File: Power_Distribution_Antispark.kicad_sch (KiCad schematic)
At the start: 87 parts, among them J1 STM Signal Conn, J2 +48V Battery Conn, J3 Motor Conn, Q1 BUK9M42-60EX, Q2 G20P06K, Q3 BUK9M42-60EX, Q4 G20P06K, U1 TLV74033PDBVR, U2 74LVC1G14GW_125, U3 TPP60308-ES1R-S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

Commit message: component layout
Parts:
- added TP1, TP10, TP11, TP12, TP2, TP3, TP4, TP5, TP6, TP7, TP8, TP9: TestPoint, TestPoint:TestPoint_Pad_D1.0mm, symbol Connector:TestPoint
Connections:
- net +3V3: now also TP12.1
- net C_Sense_12V_1: now also TP8.1
- net C_Sense_12V_2: now also TP9.1
- net C_Sense_12V_3: now also TP10.1
- net C_Sense_3V3: now also TP4.1
- net C_Sense_3V3_STM: now also TP3.1
- net C_Sense_5V_1: now also TP5.1
- net C_Sense_5V_2: now also TP6.1
- net C_Sense_5V_3: now also TP7.1
- net PreCharge_Sense: now also TP11.1
- net V_S_12V_Output: now also TP1.1
- net V_S_5V_Output: now also TP2.1

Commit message: all traces
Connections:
- net C_Sense_12V_1: now also J1.6 (Pin_6); no longer J1.4 (Pin_4)
- net GND: now also J1.5 (Pin_5); no longer J1.6 (Pin_6)
- net V_S_12V_Output: now also J1.4 (Pin_4); no longer J1.5 (Pin_5)
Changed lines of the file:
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@@
 	)
 	(junction
-		(at 85.09 356.87)
-		(diameter 0)
-		(color 0 0 0 0)
-	)
-	(junction
 		(at 60.96 369.57)
 		(diameter 0)
@@
 	)
 	(junction
+		(at 35.56 349.25)
+		(diameter 0)
+		(color 0 0 0 0)
+	)
+	(junction
 		(at 231.14 137.16)
 		(diameter 0)
@@
 	(wire
 		(pts
-			(xy 35.56 346.71) (xy 35.56 354.33)
+			(xy 35.56 346.71) (xy 35.56 349.25)
 		)
 		(stroke
@@
 		)
 	)
-	(wire
-		(pts
-			(xy 85.09 349.25) (xy 67.31 349.25)
-		)
-		(stroke
-			(width 0)
-			(type default)
-		)
-	)
 	(polyline
 		(pts
@@
 	(wire
 		(pts
+			(xy 35.56 349.25) (xy 35.56 354.33)
+		)
+		(stroke
+			(width 0)
+			(type default)
+		)
+	)
+	(wire
+		(pts
 			(xy 66.04 142.24) (xy 68.58 142.24)
 		)
@@
 	(wire
 		(pts
-			(xy 85.09 356.87) (xy 85.09 349.25)
-		)
-		(stroke
-			(width 0)
-			(type default)
-		)
-	)
-	(wire
-		(pts
 			(xy 119.38 168.91) (xy 119.38 171.45)
 		)
@@
 	(wire
 		(pts
+			(xy 35.56 349.25) (xy 54.61 349.25)
+		)
+		(stroke
+			(width 0)
+			(type default)
+		)
+	)
+	(wire
+		(pts
 			(xy 369.57 356.87) (xy 369.57 363.22)
 		)
@@
 	)
 	(label "V_S_12V_Output"
-		(at 54.61 349.25 180)
+		(at 67.31 346.71 0)
 		(effects
 			(font
 				(size 1.27 1.27)
 			)
-			(justify right bottom)
+			(justify left bottom)
 		)
 	)
@@
 		)
 	)
-	(label "C_Sense_12V_1"
-		(at 67.31 346.71 0)
-		(effects
-			(font
-				(size 1.27 1.27)
-			)
-			(justify left bottom)
-		)
-	)
 	(label "C_Sense_12V_2"
 		(at 67.31 359.41 0)
@@
 		(effects
 			(font
+				(size 1.27 1.27)
+			)
+			(justify left bottom)
+		)
+	)
+	(label "C_Sense_12V_1"
+		(at 67.31 349.25 0)
+		(effects
+			(font

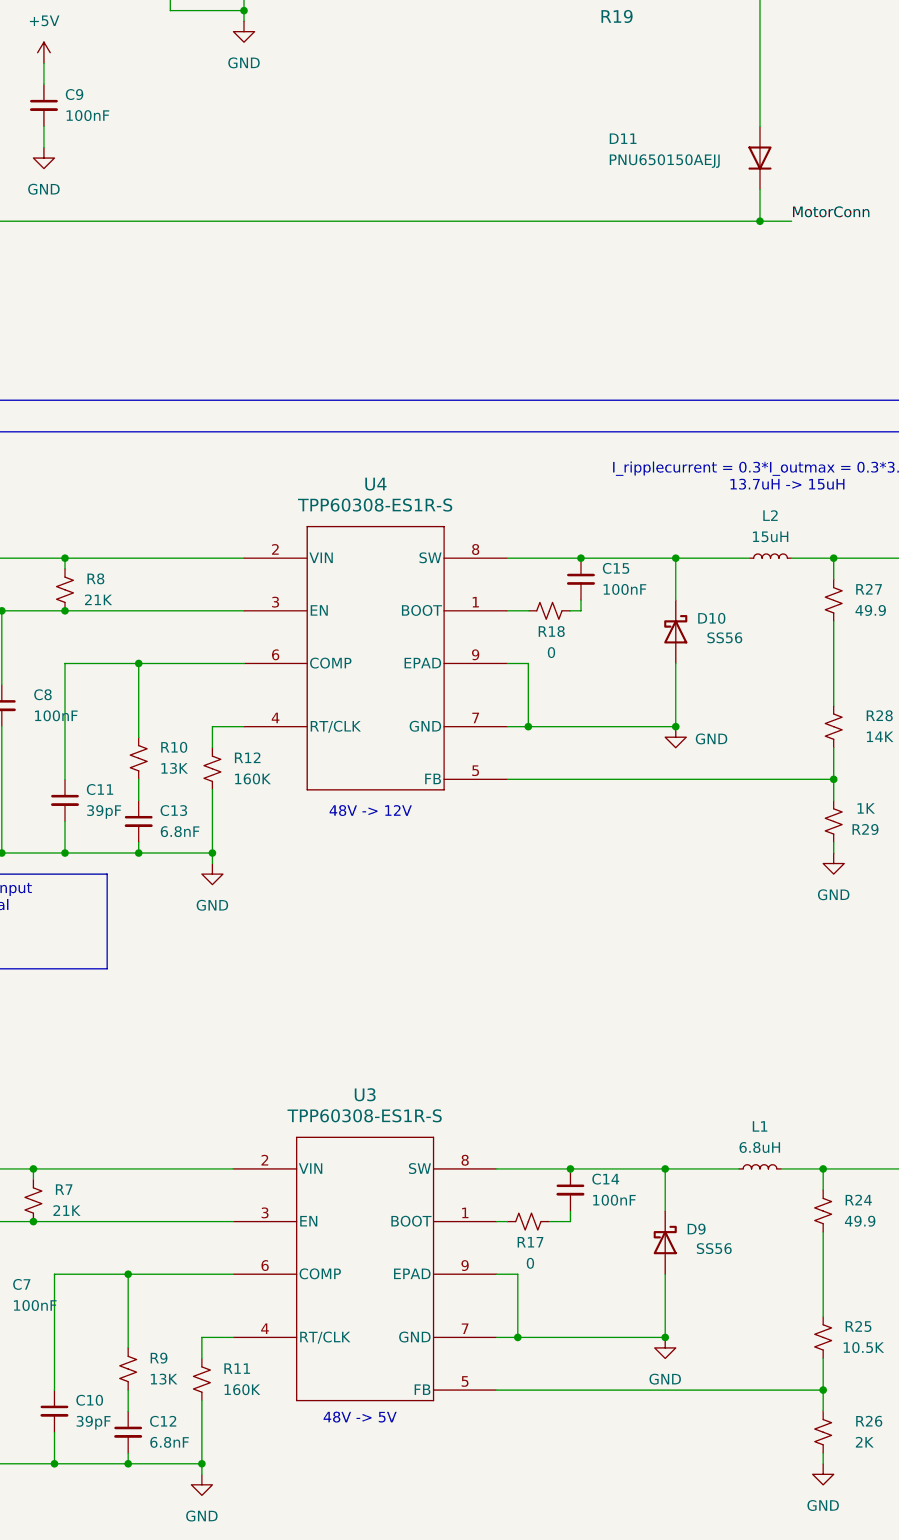
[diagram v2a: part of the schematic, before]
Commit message: fixed silkscreens
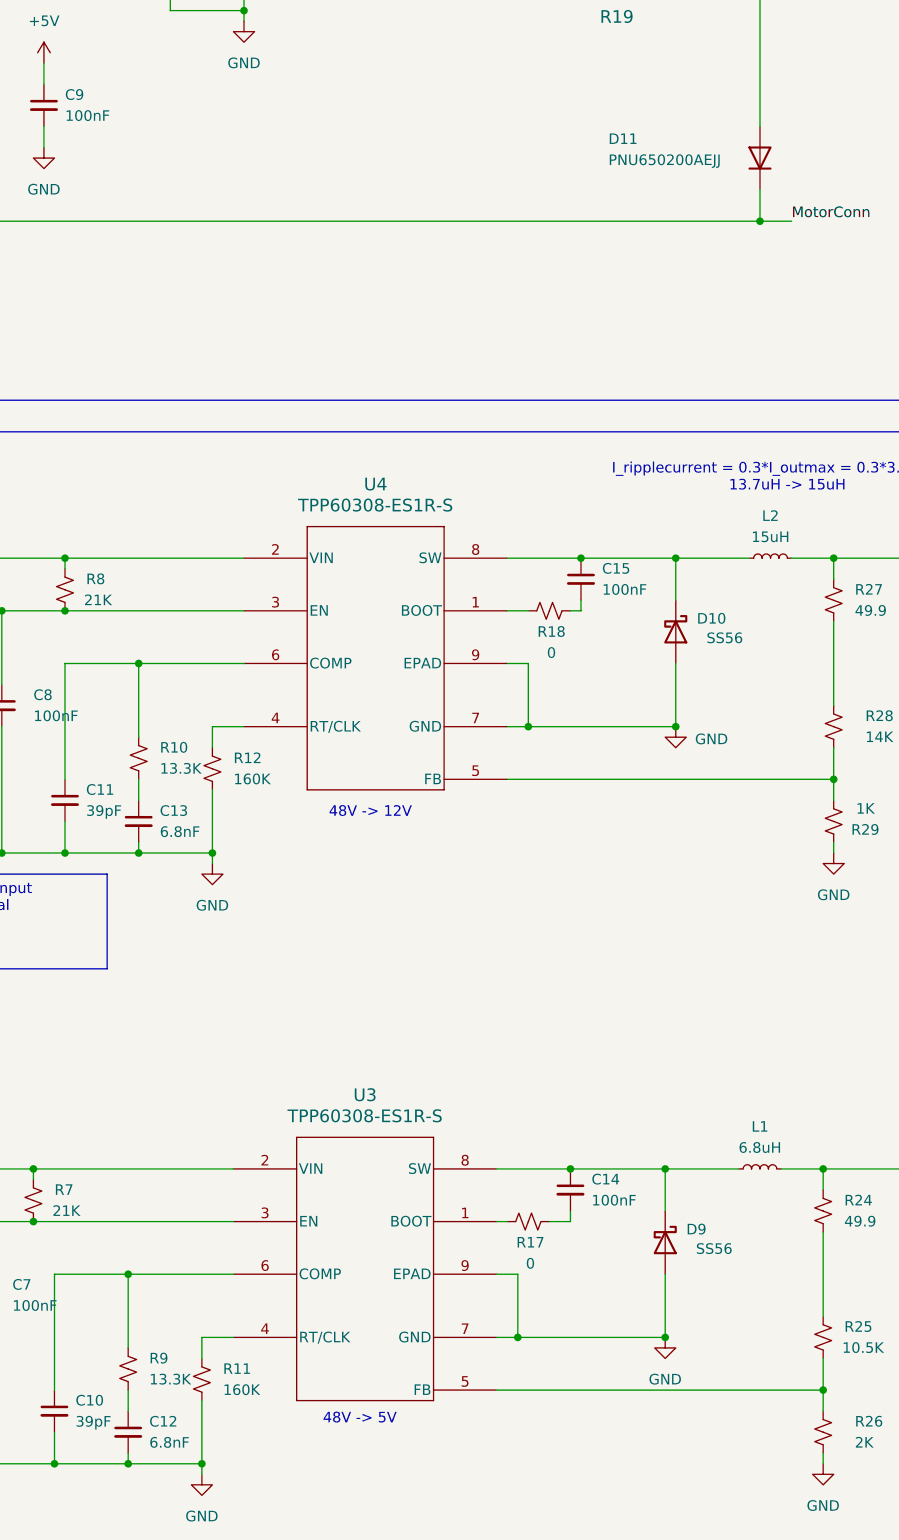
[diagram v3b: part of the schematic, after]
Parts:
- D11: value PNU650150AEJJ -> PNU650200AEJJ
- R10, R9: value 13K -> 13.3K

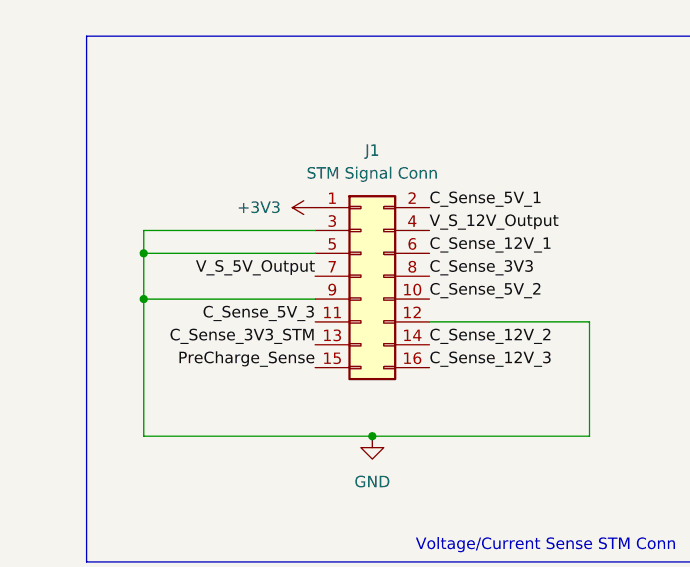
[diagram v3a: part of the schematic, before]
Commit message: fixed connectors
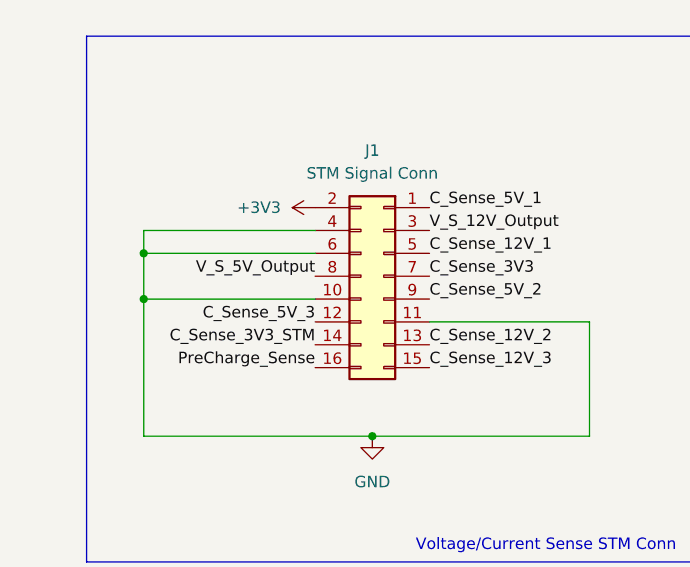
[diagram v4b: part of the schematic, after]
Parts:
- J1: footprint CustomFootprintLibrary:ADAM_2PH2-16-UA -> CustomFootprintLibrary:CONN16_B16B-PHDSS_JST
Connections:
- net +3V3: now also J1.2 (Pin_2); no longer J1.1 (Pin_1)
- net C_Sense_12V_1: now also J1.5 (Pin_5); no longer J1.6 (Pin_6)
- net C_Sense_12V_2: now also J1.13 (Pin_13); no longer J1.14 (Pin_14)
- net C_Sense_12V_3: now also J1.15 (Pin_15); no longer J1.16 (Pin_16)
- net C_Sense_3V3: now also J1.7 (Pin_7); no longer J1.8 (Pin_8)
- net C_Sense_3V3_STM: now also J1.14 (Pin_14); no longer J1.13 (Pin_13)
- net C_Sense_5V_1: now also J1.1 (Pin_1); no longer J1.2 (Pin_2)
- net C_Sense_5V_2: now also J1.9 (Pin_9); no longer J1.10 (Pin_10)
- net C_Sense_5V_3: now also J1.12 (Pin_12); no longer J1.11 (Pin_11)
- net GND: now also J1.10 (Pin_10), J1.11 (Pin_11), J1.4 (Pin_4), J1.6 (Pin_6); no longer J1.12 (Pin_12), J1.3 (Pin_3), J1.5 (Pin_5), J1.9 (Pin_9)
- net PreCharge_Sense: now also J1.16 (Pin_16); no longer J1.15 (Pin_15)
- net V_S_12V_Output: now also J1.3 (Pin_3); no longer J1.4 (Pin_4)
- net V_S_5V_Output: now also J1.8 (Pin_8); no longer J1.7 (Pin_7)
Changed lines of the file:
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@@
 	(wire
 		(pts
+			(xy 35.56 346.71) (xy 54.61 346.71)
+		)
+		(stroke
+			(width 0)
+			(type default)
+		)
+	)
+	(wire
+		(pts
 			(xy 119.38 176.53) (xy 119.38 177.8)
 		)
@@
 	(wire
 		(pts
-			(xy 54.61 346.71) (xy 35.56 346.71)
-		)
-		(stroke
-			(width 0)
-			(type default)
-		)
-	)
-	(wire
-		(pts
 			(xy 231.14 142.24) (xy 231.14 143.51)
 		)
@@
 	(symbol
 		(lib_id "Connector_Generic:Conn_02x08_Odd_Even")
-		(at 59.69 351.79 0)
+		(at 62.23 351.79 0)
+		(mirror y)
 		(unit 1)
 		(exclude_from_sim no)
@@
 		(on_board yes)
 		(dnp no)
-		(fields_autoplaced yes)
 		(property "Reference" "J1"
 			(at 60.96 337.82 0)
@@
 			)
 		)
-		(property "Footprint" "CustomFootprintLibrary:ADAM_2PH2-16-UA"
-			(at 59.69 351.79 0)
+		(property "Footprint" "CustomFootprintLibrary:CONN16_B16B-PHDSS_JST"
+			(at 62.23 351.79 0)
 			(effects
 				(font
@@
 			)
 		)
-		(property "Datasheet" "https://www.digikey.ca/en/products/detail/adam-tech/2PH2-16-UA/9830539"
-			(at 59.69 351.79 0)
+		(property "Datasheet" "https://www.digikey.ca/en/products/detail/jst-sales-america-inc/B16B-PHDSS/926671"
+			(at 62.23 351.79 0)
 			(effects
 				(font
@@
 		)
 		(property "Description" "CONN HEADER VERT 16POS 2MM"
-			(at 59.69 351.79 0)
+			(at 62.23 351.79 0)
 			(effects
 				(font
@@
 		)
 		(property "Sim.Type" ""
-			(at 59.69 351.79 0)
+			(at 62.23 351.79 0)
 			(effects
 				(font

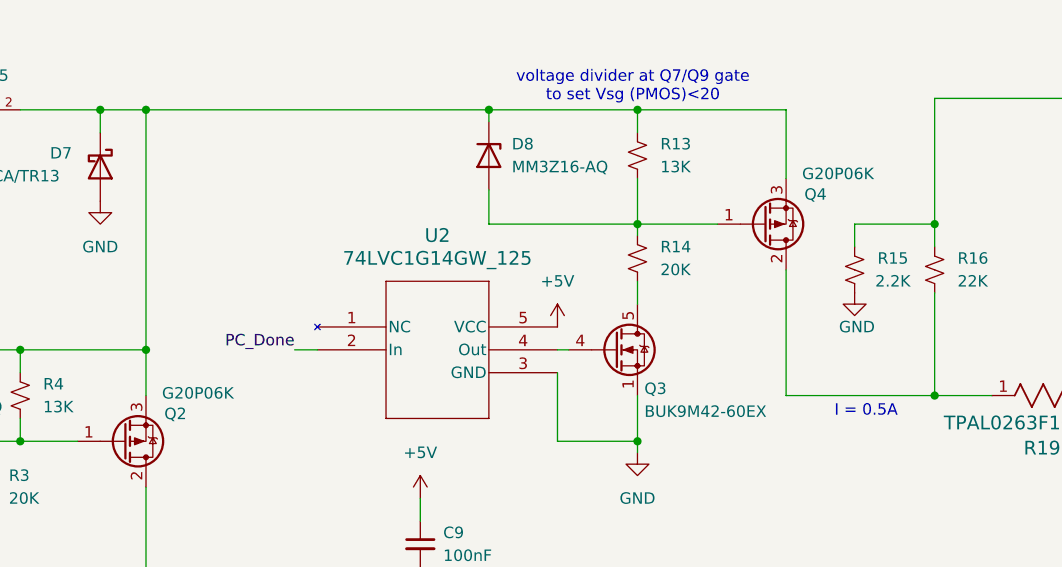
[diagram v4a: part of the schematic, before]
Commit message: changed main pmos
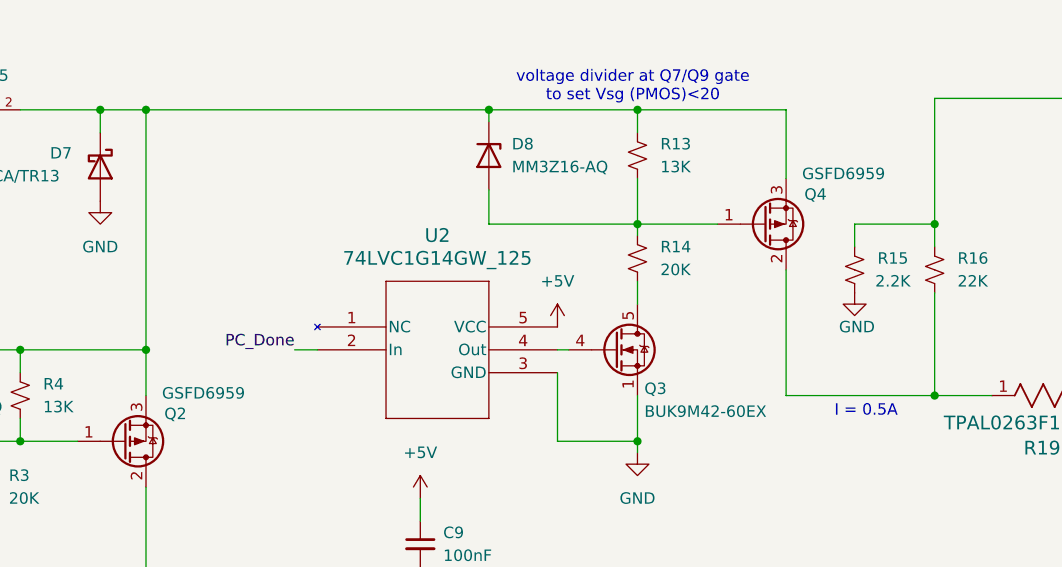
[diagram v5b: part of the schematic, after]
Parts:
- Q2, Q4: value G20P06K -> GSFD6959
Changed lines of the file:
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@@
 			)
 		)
-		(property "Value" "G20P06K"
+		(property "Value" "GSFD6959"
 			(at 150.368 46.482 0)
 			(effects
@@
 			)
 		)
-		(property "Datasheet" "https://www.digikey.ca/en/products/detail/goford-semiconductor/G20P06K/16689207"
+		(property "Datasheet" "https://www.digikey.ca/en/products/detail/good-ark-semiconductor/GSFD6959/21275302"
 			(at 151.13 48.26 0)
 			(effects
@@
 			)
 		)
-		(property "Description" "P-Channel 60 V 20A (Tc) 90W (Tc) Surface Mount TO-252"
+		(property "Description" "MOSFET, P-CH, SINGLE, -60.00A, -"
 			(at 146.05 52.07 0)
 			(effects
@@
 			)
 		)
-		(property "Value" "G20P06K"
+		(property "Value" "GSFD6959"
 			(at 79.248 70.866 0)
 			(effects
@@
 			)
 		)
-		(property "Datasheet" "https://www.digikey.ca/en/products/detail/goford-semiconductor/G20P06K/16689207"
+		(property "Datasheet" "https://www.digikey.ca/en/products/detail/good-ark-semiconductor/GSFD6959/21275302"
 			(at 80.01 72.39 0)
 			(effects
@@
 			)
 		)
-		(property "Description" "P-Channel 60 V 20A (Tc) 90W (Tc) Surface Mount TO-252"
+		(property "Description" "MOSFET, P-CH, SINGLE, -60.00A, -"
 			(at 74.93 76.2 0)
 			(effects
